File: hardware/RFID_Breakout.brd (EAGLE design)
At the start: 25.4 x 25.4 mm, 6 parts, among them U1 RFID

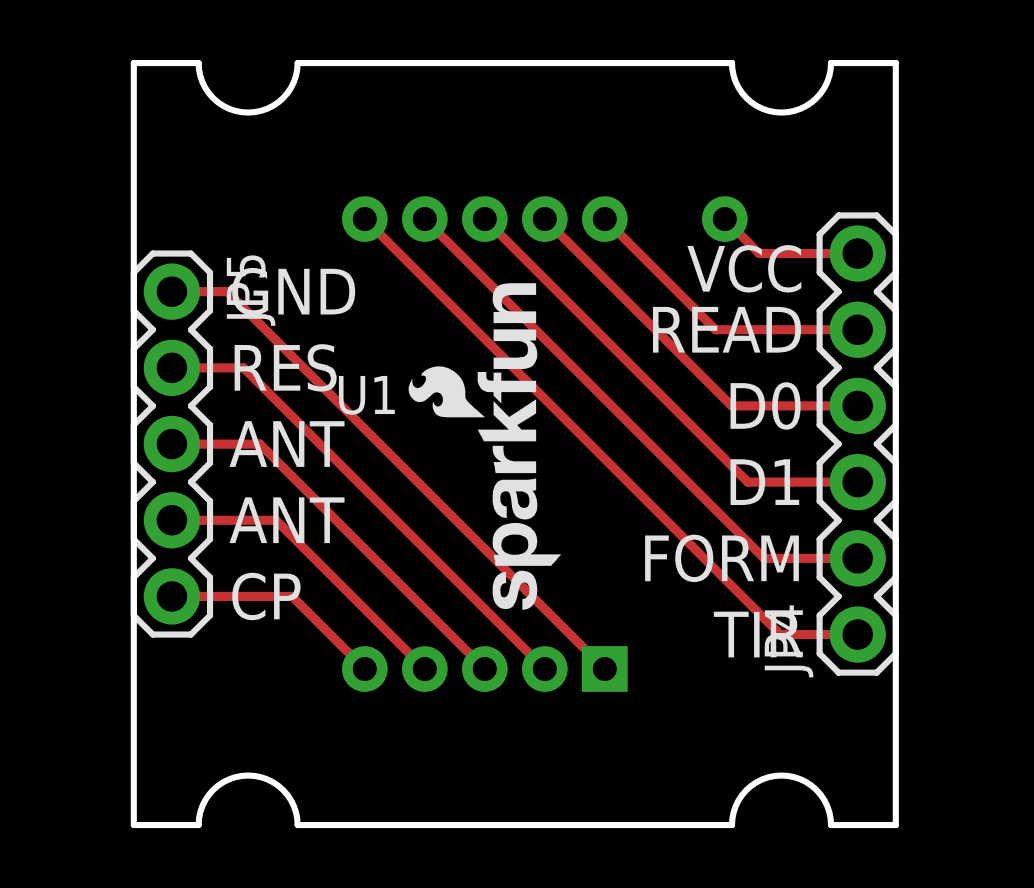
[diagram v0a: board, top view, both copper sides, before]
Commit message: Corrected layout to work with breadboard.
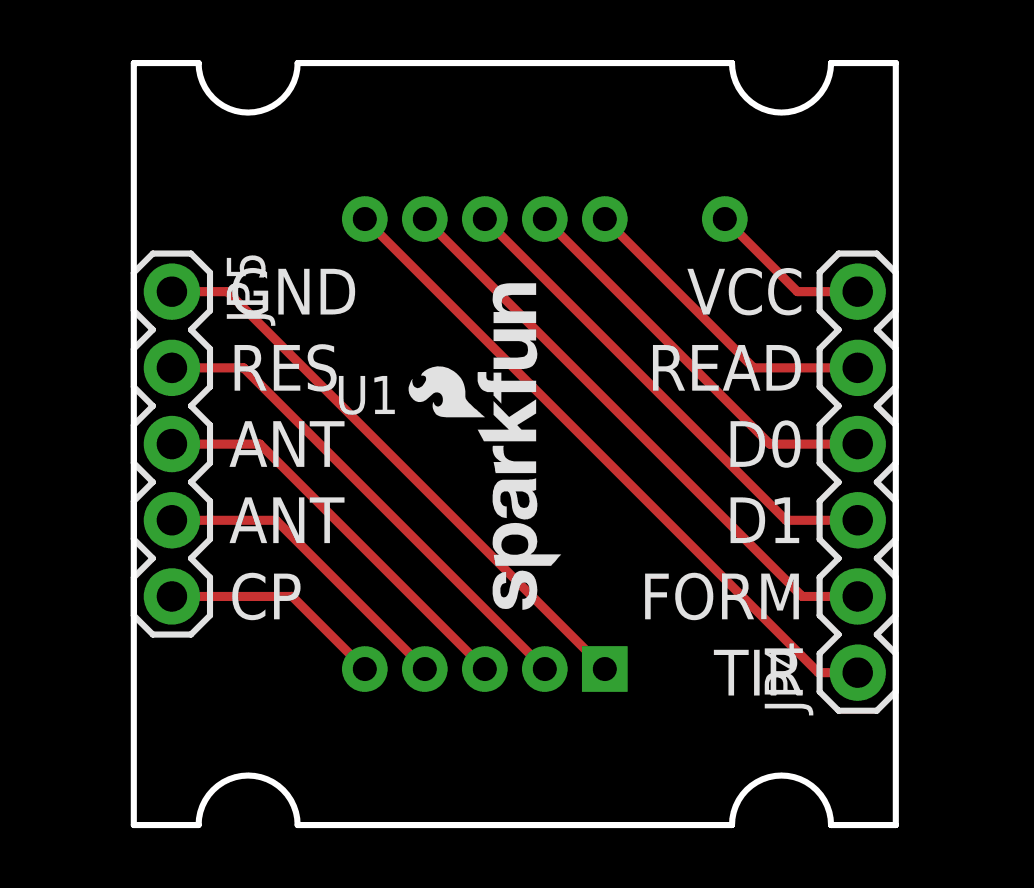
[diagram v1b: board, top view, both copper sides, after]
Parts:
- moved JP4 1.27 mm to (11.4, -7.62)
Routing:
- net READ: track 9.96 -> 10.5 mm
- net VCC: track 4.91 -> 5.43 mm
- net TIR: track 22.2 -> 22.7 mm
- net FORM: track 19.1 -> 19.6 mm
- net D1: track 16.1 -> 16.6 mm
- net D0: track 13.0 -> 13.5 mm
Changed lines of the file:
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@@
 <layer number="47" name="Measures" color="7" fill="1" visible="no" active="yes"/>
 <layer number="48" name="Document" color="7" fill="1" visible="no" active="yes"/>
-<layer number="49" name="Reference" color="7" fill="1" visible="yes" active="yes"/>
+<layer number="49" name="Reference" color="7" fill="1" visible="no" active="yes"/>
 <layer number="50" name="dxf" color="7" fill="1" visible="no" active="no"/>
 <layer number="51" name="tDocu" color="6" fill="1" visible="yes" active="yes"/>
@@
 <text x="-9.525" y="-3.302" size="1.524" layer="21" font="vector" ratio="15">ANT</text>
 <text x="-9.525" y="-5.842" size="1.524" layer="21" font="vector" ratio="15">CP</text>
-<text x="9.652" y="6.604" size="1.524" layer="21" font="vector" ratio="15" rot="R180">VCC</text>
-<text x="9.652" y="4.572" size="1.524" layer="21" font="vector" ratio="15" rot="R180">READ</text>
-<text x="9.652" y="2.032" size="1.524" layer="21" font="vector" ratio="15" rot="R180">D0</text>
-<text x="9.652" y="-0.508" size="1.524" layer="21" font="vector" ratio="15" rot="R180">D1</text>
-<text x="9.652" y="-3.048" size="1.524" layer="21" font="vector" ratio="15" rot="R180">FORM</text>
-<text x="9.652" y="-5.588" size="1.524" layer="21" font="vector" ratio="15" rot="R180">TIR</text>
+<text x="9.652" y="5.842" size="1.524" layer="21" font="vector" ratio="15" rot="R180">VCC</text>
+<text x="9.652" y="3.302" size="1.524" layer="21" font="vector" ratio="15" rot="R180">READ</text>
+<text x="9.652" y="0.762" size="1.524" layer="21" font="vector" ratio="15" rot="R180">D0</text>
+<text x="9.652" y="-1.778" size="1.524" layer="21" font="vector" ratio="15" rot="R180">D1</text>
+<text x="9.652" y="-4.318" size="1.524" layer="21" font="vector" ratio="15" rot="R180">FORM</text>
+<text x="9.652" y="-6.858" size="1.524" layer="21" font="vector" ratio="15" rot="R180">TIR</text>
 <wire x1="9.652" y1="7.874" x2="9.652" y2="-8.001" width="0.2032" layer="51"/>
 <text x="6.858" y="-3.81" size="1.27" layer="22" font="vector" ratio="15" rot="MR0">RFID Breakout</text>
@@
 <element name="LOGO1" library="SparkFun-Aesthetics" package="SFE_LOGO_NAME_FLAME_.1" value="SFE_LOGO_NAME_FLAME.1_INCH" x="5.842" y="-1.651" rot="MR0"/>
 <element name="FRAME1" library="SparkFun-Aesthetics" package="CREATIVE_COMMONS" value="FRAME-LETTER" x="-36.83" y="-30.48"/>
-<element name="JP4" library="SparkFun-Connectors" package="1X06" value="" x="11.43" y="-6.35" rot="R90"/>
+<element name="JP4" library="SparkFun-Connectors" package="1X06" value="" x="11.43" y="-7.62" rot="R90"/>
 <element name="JP5" library="SparkFun-Connectors" package="1X05" value="" x="-11.43" y="5.08" rot="R270"/>
 <element name="LOGO2" library="SparkFun-Aesthetics" package="SFE_LOGO_NAME_FLAME_.1" value="SFE_LOGO_NAME_FLAME.1_INCH" x="1.651" y="-5.969" rot="R90"/>
@@
 <contactref element="U1" pad="10"/>
 <contactref element="JP4" pad="5"/>
-<wire x1="3" y1="7.5" x2="6.69" y2="3.81" width="0.3048" layer="1"/>
-<wire x1="6.69" y1="3.81" x2="11.43" y2="3.81" width="0.3048" layer="1"/>
+<wire x1="3" y1="7.5" x2="7.96" y2="2.54" width="0.3048" layer="1"/>
+<wire x1="7.96" y1="2.54" x2="11.43" y2="2.54" width="0.3048" layer="1"/>
 </signal>
 <signal name="D0">
 <contactref element="U1" pad="9"/>
 <contactref element="JP4" pad="4"/>
-<wire x1="1" y1="7.5" x2="7.23" y2="1.27" width="0.3048" layer="1"/>
-<wire x1="7.23" y1="1.27" x2="11.43" y2="1.27" width="0.3048" layer="1"/>
+<wire x1="1" y1="7.5" x2="8.5" y2="0" width="0.3048" layer="1"/>
+<wire x1="8.5" y1="0" x2="11.43" y2="0" width="0.3048" layer="1"/>
 </signal>
 <signal name="D1">
 <contactref element="U1" pad="8"/>
 <contactref element="JP4" pad="3"/>
-<wire x1="-1" y1="7.5" x2="7.77" y2="-1.27" width="0.3048" layer="1"/>
-<wire x1="7.77" y1="-1.27" x2="11.43" y2="-1.27" width="0.3048" layer="1"/>
+<wire x1="-1" y1="7.5" x2="9.04" y2="-2.54" width="0.3048" layer="1"/>
+<wire x1="9.04" y1="-2.54" x2="11.43" y2="-2.54" width="0.3048" layer="1"/>
 </signal>
 <signal name="FORM">
 <contactref element="U1" pad="7"/>
 <contactref element="JP4" pad="2"/>
-<wire x1="-3" y1="7.5" x2="8.31" y2="-3.81" width="0.3048" layer="1"/>
-<wire x1="8.31" y1="-3.81" x2="11.43" y2="-3.81" width="0.3048" layer="1"/>
+<wire x1="-3" y1="7.5" x2="9.58" y2="-5.08" width="0.3048" layer="1"/>
+<wire x1="9.58" y1="-5.08" x2="11.43" y2="-5.08" width="0.3048" layer="1"/>
 </signal>
 <signal name="TIR">
 <contactref element="U1" pad="6"/>
 <contactref element="JP4" pad="1"/>
-<wire x1="-5" y1="7.5" x2="8.85" y2="-6.35" width="0.3048" layer="1"/>
-<wire x1="8.85" y1="-6.35" x2="11.43" y2="-6.35" width="0.3048" layer="1"/>
+<wire x1="-5" y1="7.5" x2="10.12" y2="-7.62" width="0.3048" layer="1"/>
+<wire x1="10.12" y1="-7.62" x2="11.43" y2="-7.62" width="0.3048" layer="1"/>
 </signal>
 <signal name="VCC">
 <contactref element="U1" pad="11"/>
 <contactref element="JP4" pad="6"/>
-<wire x1="7" y1="7.5" x2="8.15" y2="6.35" width="0.3048" layer="1"/>
-<wire x1="8.15" y1="6.35" x2="11.43" y2="6.35" width="0.3048" layer="1"/>
+<wire x1="7" y1="7.5" x2="9.42" y2="5.08" width="0.3048" layer="1"/>
+<wire x1="9.42" y1="5.08" x2="11.43" y2="5.08" width="0.3048" layer="1"/>
 </signal>
 <signal name="GND">

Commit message: Reversed layout to make labels visible when attached.
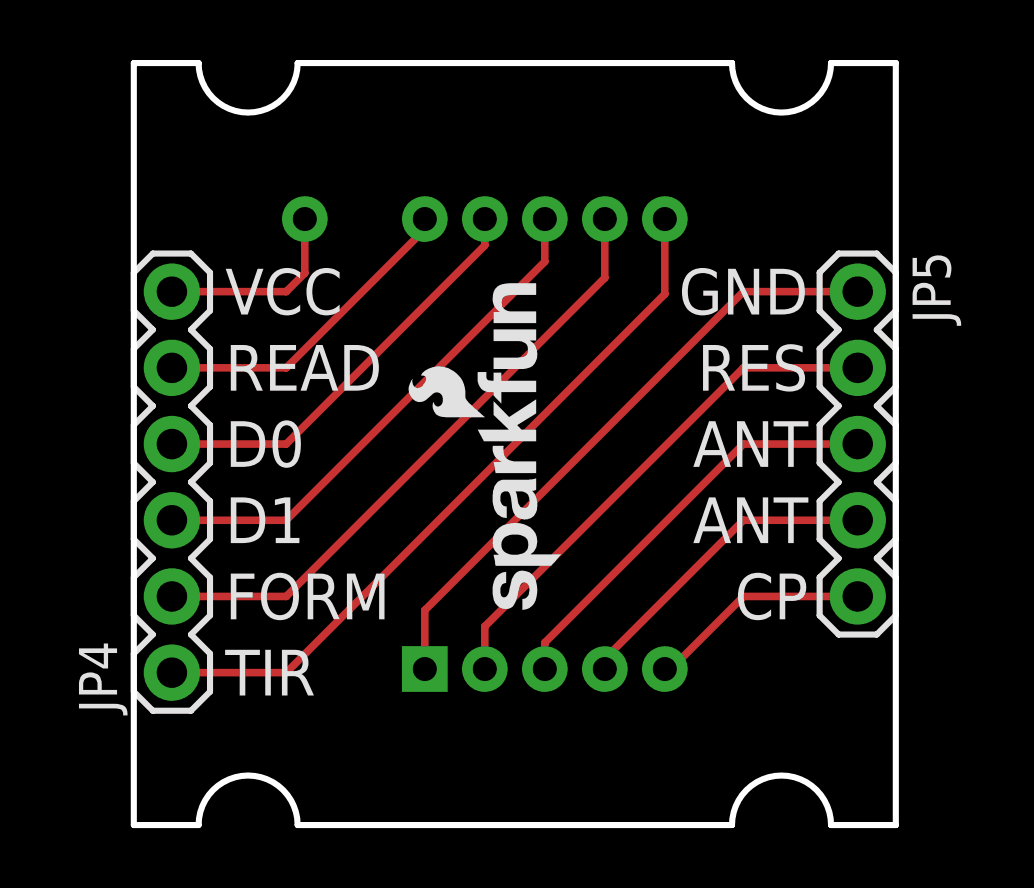
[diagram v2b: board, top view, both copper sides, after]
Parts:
- moved JP4 22.9 mm to (-11.4, -7.62)
- moved JP5 22.9 mm to (11.4, 5.08)
- flipped U1 to the bottom
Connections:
- net GND renamed N$3
- net VCC renamed N$2
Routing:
- net TIR: track 22.7 -> 24.2 mm
- net N$3: track 19.6 -> 20.8 mm
- net FORM: track 19.6 -> 20.8 mm
- net N$2: track 5.43 -> 6.49 mm
- net RES: track 16.6 -> 17.4 mm
- net D1: track 16.6 -> 17.4 mm
- net D0: track 13.5 -> 14.1 mm
- net ANT1: track 13.5 -> 14.1 mm
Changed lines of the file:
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@@
 <layer number="50" name="dxf" color="7" fill="1" visible="no" active="no"/>
 <layer number="51" name="tDocu" color="6" fill="1" visible="yes" active="yes"/>
-<layer number="52" name="bDocu" color="7" fill="1" visible="no" active="yes"/>
+<layer number="52" name="bDocu" color="7" fill="1" visible="yes" active="yes"/>
 <layer number="53" name="tGND_GNDA" color="7" fill="9" visible="no" active="no"/>
 <layer number="54" name="bGND_GNDA" color="1" fill="9" visible="no" active="no"/>
@@
 <wire x1="-10.541" y1="12.7" x2="-12.7" y2="12.7" width="0.2032" layer="20"/>
 <wire x1="-12.7" y1="12.7" x2="-12.7" y2="-12.7" width="0.2032" layer="20"/>
-<text x="-9.525" y="4.318" size="1.524" layer="21" font="vector" ratio="15">GND</text>
-<text x="-9.525" y="1.778" size="1.524" layer="21" font="vector" ratio="15">RES</text>
-<text x="-9.525" y="-0.762" size="1.524" layer="21" font="vector" ratio="15">ANT</text>
-<text x="-9.525" y="-3.302" size="1.524" layer="21" font="vector" ratio="15">ANT</text>
-<text x="-9.525" y="-5.842" size="1.524" layer="21" font="vector" ratio="15">CP</text>
-<text x="9.652" y="5.842" size="1.524" layer="21" font="vector" ratio="15" rot="R180">VCC</text>
-<text x="9.652" y="3.302" size="1.524" layer="21" font="vector" ratio="15" rot="R180">READ</text>
-<text x="9.652" y="0.762" size="1.524" layer="21" font="vector" ratio="15" rot="R180">D0</text>
-<text x="9.652" y="-1.778" size="1.524" layer="21" font="vector" ratio="15" rot="R180">D1</text>
-<text x="9.652" y="-4.318" size="1.524" layer="21" font="vector" ratio="15" rot="R180">FORM</text>
-<text x="9.652" y="-6.858" size="1.524" layer="21" font="vector" ratio="15" rot="R180">TIR</text>
-<wire x1="9.652" y1="7.874" x2="9.652" y2="-8.001" width="0.2032" layer="51"/>
+<text x="9.779" y="5.842" size="1.524" layer="21" font="vector" ratio="15" rot="R180">GND</text>
+<text x="9.779" y="3.302" size="1.524" layer="21" font="vector" ratio="15" rot="R180">RES</text>
+<text x="9.779" y="0.762" size="1.524" layer="21" font="vector" ratio="15" rot="R180">ANT</text>
+<text x="9.779" y="-1.778" size="1.524" layer="21" font="vector" ratio="15" rot="R180">ANT</text>
+<text x="9.779" y="-4.318" size="1.524" layer="21" font="vector" ratio="15" rot="R180">CP</text>
+<text x="-9.652" y="4.318" size="1.524" layer="21" font="vector" ratio="15">VCC</text>
+<text x="-9.652" y="1.778" size="1.524" layer="21" font="vector" ratio="15">READ</text>
+<text x="-9.652" y="-0.762" size="1.524" layer="21" font="vector" ratio="15">D0</text>
+<text x="-9.652" y="-3.302" size="1.524" layer="21" font="vector" ratio="15">D1</text>
+<text x="-9.652" y="-5.842" size="1.524" layer="21" font="vector" ratio="15">FORM</text>
+<text x="-9.652" y="-8.382" size="1.524" layer="21" font="vector" ratio="15">TIR</text>
 <text x="6.858" y="-3.81" size="1.27" layer="22" font="vector" ratio="15" rot="MR0">RFID Breakout</text>
 <wire x1="-10.541" y1="12.7" x2="-7.239" y2="12.7" width="0.2032" layer="20" curve="180"/>
@@
 </autorouter>
 <elements>
-<element name="U1" library="ID Innovations" package="ID_PACKAGE" value="RFID" x="0" y="0"/>
+<element name="U1" library="ID Innovations" package="ID_PACKAGE" value="RFID" x="0" y="0" rot="MR0"/>
 <element name="LOGO1" library="SparkFun-Aesthetics" package="SFE_LOGO_NAME_FLAME_.1" value="SFE_LOGO_NAME_FLAME.1_INCH" x="5.842" y="-1.651" rot="MR0"/>
 <element name="FRAME1" library="SparkFun-Aesthetics" package="CREATIVE_COMMONS" value="FRAME-LETTER" x="-36.83" y="-30.48"/>
-<element name="JP4" library="SparkFun-Connectors" package="1X06" value="" x="11.43" y="-7.62" rot="R90"/>
-<element name="JP5" library="SparkFun-Connectors" package="1X05" value="" x="-11.43" y="5.08" rot="R270"/>
+<element name="JP4" library="SparkFun-Connectors" package="1X06" value="" x="-11.43" y="-7.62" rot="R90"/>
+<element name="JP5" library="SparkFun-Connectors" package="1X05" value="" x="11.43" y="5.08" rot="R270"/>
 <element name="LOGO2" library="SparkFun-Aesthetics" package="SFE_LOGO_NAME_FLAME_.1" value="SFE_LOGO_NAME_FLAME.1_INCH" x="1.651" y="-5.969" rot="R90"/>
 </elements>
@@
 <contactref element="U1" pad="3"/>
 <contactref element="JP5" pad="3"/>
-<wire x1="-1" y1="-7.5" x2="-8.5" y2="0" width="0.3048" layer="1"/>
-<wire x1="-8.5" y1="0" x2="-11.43" y2="0" width="0.3048" layer="1"/>
+<wire x1="1" y1="-7.5" x2="1" y2="-6.62" width="0.254" layer="1"/>
+<wire x1="1" y1="-6.62" x2="7.62" y2="0" width="0.254" layer="1"/>
+<wire x1="7.62" y1="0" x2="11.43" y2="0" width="0.254" layer="1"/>
 </signal>
 <signal name="ANT2">
 <contactref element="U1" pad="4"/>
 <contactref element="JP5" pad="4"/>
-<wire x1="-3" y1="-7.5" x2="-7.96" y2="-2.54" width="0.3048" layer="1"/>
-<wire x1="-7.96" y1="-2.54" x2="-11.43" y2="-2.54" width="0.3048" layer="1"/>
+<wire x1="3" y1="-7.5" x2="3" y2="-7.16" width="0.254" layer="1"/>
+<wire x1="3" y1="-7.16" x2="7.62" y2="-2.54" width="0.254" layer="1"/>
+<wire x1="7.62" y1="-2.54" x2="11.43" y2="-2.54" width="0.254" layer="1"/>
 </signal>
 <signal name="CP">
 <contactref element="U1" pad="5"/>
 <contactref element="JP5" pad="5"/>
-<wire x1="-5" y1="-7.5" x2="-7.42" y2="-5.08" width="0.3048" layer="1"/>
-<wire x1="-7.42" y1="-5.08" x2="-11.43" y2="-5.08" width="0.3048" layer="1"/>
+<wire x1="5" y1="-7.5" x2="5.2" y2="-7.5" width="0.254" layer="1"/>
+<wire x1="5.2" y1="-7.5" x2="7.62" y2="-5.08" width="0.254" layer="1"/>
+<wire x1="7.62" y1="-5.08" x2="11.43" y2="-5.08" width="0.254" layer="1"/>
 </signal>
 <signal name="RES">
 <contactref element="U1" pad="2"/>
 <contactref element="JP5" pad="2"/>
-<wire x1="1" y1="-7.5" x2="-9.04" y2="2.54" width="0.3048" layer="1"/>
-<wire x1="-9.04" y1="2.54" x2="-11.43" y2="2.54" width="0.3048" layer="1"/>
+<wire x1="-1" y1="-7.5" x2="-1" y2="-6.08" width="0.254" layer="1"/>
+<wire x1="-1" y1="-6.08" x2="7.62" y2="2.54" width="0.254" layer="1"/>
+<wire x1="7.62" y1="2.54" x2="11.43" y2="2.54" width="0.254" layer="1"/>
 </signal>
 <signal name="READ">
 <contactref element="U1" pad="10"/>
 <contactref element="JP4" pad="5"/>
-<wire x1="3" y1="7.5" x2="7.96" y2="2.54" width="0.3048" layer="1"/>
-<wire x1="7.96" y1="2.54" x2="11.43" y2="2.54" width="0.3048" layer="1"/>
+<wire x1="-3" y1="7.5" x2="-3" y2="7.16" width="0.254" layer="1"/>
+<wire x1="-3" y1="7.16" x2="-7.62" y2="2.54" width="0.254" layer="1"/>
+<wire x1="-7.62" y1="2.54" x2="-11.43" y2="2.54" width="0.254" layer="1"/>
 </signal>
 <signal name="D0">
 <contactref element="U1" pad="9"/>
 <contactref element="JP4" pad="4"/>
-<wire x1="1" y1="7.5" x2="8.5" y2="0" width="0.3048" layer="1"/>
-<wire x1="8.5" y1="0" x2="11.43" y2="0" width="0.3048" layer="1"/>
+<wire x1="-1" y1="7.5" x2="-1" y2="6.62" width="0.254" layer="1"/>
+<wire x1="-1" y1="6.62" x2="-7.62" y2="0" width="0.254" layer="1"/>
+<wire x1="-7.62" y1="0" x2="-11.43" y2="0" width="0.254" layer="1"/>
 </signal>
 <signal name="D1">
 <contactref element="U1" pad="8"/>
 <contactref element="JP4" pad="3"/>
-<wire x1="-1" y1="7.5" x2="9.04" y2="-2.54" width="0.3048" layer="1"/>
-<wire x1="9.04" y1="-2.54" x2="11.43" y2="-2.54" width="0.3048" layer="1"/>
+<wire x1="1" y1="7.5" x2="1" y2="6.08" width="0.254" layer="1"/>
+<wire x1="1" y1="6.08" x2="-7.62" y2="-2.54" width="0.254" layer="1"/>
+<wire x1="-7.62" y1="-2.54" x2="-11.43" y2="-2.54" width="0.254" layer="1"/>
 </signal>
 <signal name="FORM">
 <contactref element="U1" pad="7"/>
 <contactref element="JP4" pad="2"/>
-<wire x1="-3" y1="7.5" x2="9.58" y2="-5.08" width="0.3048" layer="1"/>
-<wire x1="9.58" y1="-5.08" x2="11.43" y2="-5.08" width="0.3048" layer="1"/>
+<wire x1="3" y1="7.5" x2="3" y2="5.54" width="0.254" layer="1"/>
+<wire x1="3" y1="5.54" x2="-7.62" y2="-5.08" width="0.254" layer="1"/>
+<wire x1="-7.62" y1="-5.08" x2="-11.43" y2="-5.08" width="0.254" layer="1"/>
 </signal>
 <signal name="TIR">
 <contactref element="U1" pad="6"/>
 <contactref element="JP4" pad="1"/>
-<wire x1="-5" y1="7.5" x2="10.12" y2="-7.62" width="0.3048" layer="1"/>
-<wire x1="10.12" y1="-7.62" x2="11.43" y2="-7.62" width="0.3048" layer="1"/>
-</signal>
-<signal name="VCC">
+<wire x1="5" y1="7.5" x2="5" y2="5" width="0.254" layer="1"/>
+<wire x1="5" y1="5" x2="-7.62" y2="-7.62" width="0.254" layer="1"/>
+<wire x1="-7.62" y1="-7.62" x2="-11.43" y2="-7.62" width="0.254" layer="1"/>
+</signal>
+<signal name="N$2">
 <contactref element="U1" pad="11"/>
 <contactref element="JP4" pad="6"/>
-<wire x1="7" y1="7.5" x2="9.42" y2="5.08" width="0.3048" layer="1"/>
-<wire x1="9.42" y1="5.08" x2="11.43" y2="5.08" width="0.3048" layer="1"/>
-</signal>
-<signal name="GND">
+<wire x1="-7" y1="7.5" x2="-7" y2="5.7" width="0.254" layer="1"/>
+<wire x1="-7" y1="5.7" x2="-7.62" y2="5.08" width="0.254" layer="1"/>
+<wire x1="-7.62" y1="5.08" x2="-11.43" y2="5.08" width="0.254" layer="1"/>
+</signal>
+<signal name="N$3">
 <contactref element="U1" pad="1"/>
 <contactref element="JP5" pad="1"/>
-<wire x1="3" y1="-7.5" x2="-9.58" y2="5.08" width="0.3048" layer="1"/>
-<wire x1="-9.58" y1="5.08" x2="-11.43" y2="5.08" width="0.3048" layer="1"/>
+<wire x1="-3" y1="-7.5" x2="-3" y2="-5.54" width="0.254" layer="1"/>
+<wire x1="-3" y1="-5.54" x2="7.62" y2="5.08" width="0.254" layer="1"/>
+<wire x1="7.62" y1="5.08" x2="11.43" y2="5.08" width="0.254" layer="1"/>
 </signal>
 </signals>
